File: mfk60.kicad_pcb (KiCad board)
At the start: 2 copper layers, 300 x 95.2 mm, 180 parts, among them J1 USB_C_Receptacle_USB2.0, J2 TRRS Jack, J3 ISP, J4 USB_C_Receptacle_USB2.0, J5 TRRS Jack, J6 ISP, SW1 COL1_ROW1, SW10 COL10_ROW1, SW11 COL11_ROW1, SW12 COL12_ROW1, SW13 COL13_ROW1, SW14 COL14_ROW1, SW15 COL1_ROW2, SW16 COL2_ROW2, SW17 COL3_ROW2, SW18 COL4_ROW2, SW19 COL5_ROW2, SW2 COL2_ROW1, SW20 COL6_ROW2, SW21 COL7_ROW2, SW22 COL8_ROW2, SW23 COL9_ROW2, SW24 COL10_ROW2, SW25 COL11_ROW2, SW26 COL12_ROW2, SW27 COL13_ROW2, SW28 COL14_ROW2, SW29 COL1_ROW3, SW3 COL3_ROW1, SW30 COL2_ROW3, SW31 COL3_ROW3, SW32 COL4_ROW3, SW33 COL5_ROW3, SW34 COL6_ROW3, SW35 COL7_ROW3, SW36 COL8_ROW3, SW37 COL9_ROW3, SW38 COL10_ROW3, SW39 COL11_ROW3, SW4 COL4_ROW1, SW40 COL12_ROW3, SW41 COL13_ROW3, SW42 COL1_ROW4, SW43 COL2_ROW4, SW44 COL3_ROW4, SW45 COL4_ROW4, SW46 COL5_ROW4, SW47 COL6_ROW4, SW48 COL7_ROW4, SW49 COL8_ROW4, SW5 COL5_ROW1, SW50 COL9_ROW4, SW51 COL10_ROW4, SW52 COL11_ROW4, SW53 COL12_ROW4, SW54 COL13_ROW4, SW55 COL1_ROW5, SW56 COL2_ROW5, SW57 COL3_ROW5, SW58 COL7_ROW5, SW59 COL8_ROW5, SW6 COL6_ROW1, SW60 COL9_ROW5, SW61 COL10_ROW5, SW62 RST, SW63 RST, SW7 COL7_ROW1, SW8 COL8_ROW1, SW9 COL9_ROW1, T1 Tab, T2 Tab, T3 Tab, T4 Tab, T5 Tab, T6 Tab, T7 Tab, U1 ATmega32U4-M, U2 ATmega32U4-M, Y1 16M, Y2 16M

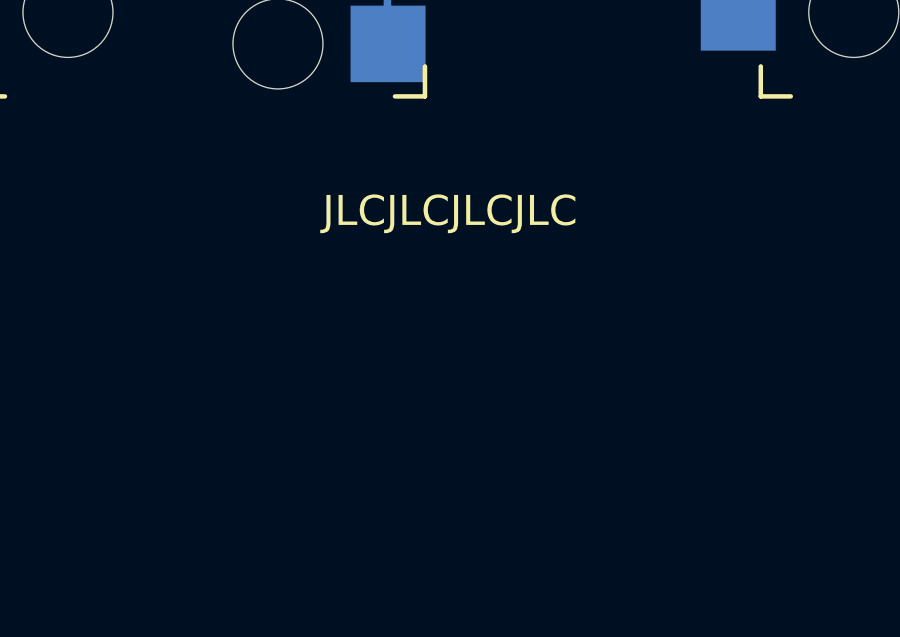
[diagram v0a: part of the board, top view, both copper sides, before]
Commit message: Adjust JLC text position and add it to script.
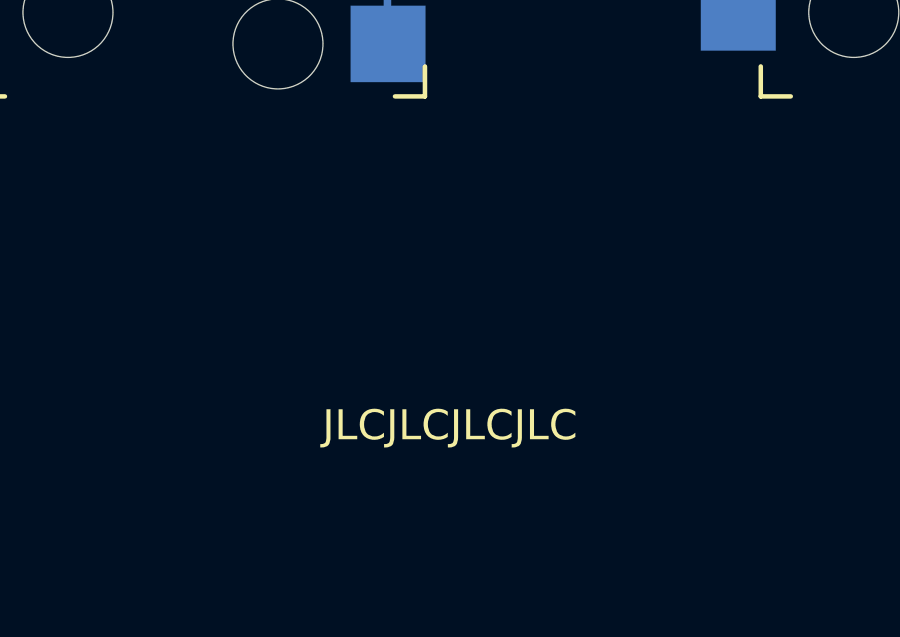
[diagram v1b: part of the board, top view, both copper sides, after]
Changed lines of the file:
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@@
     (effects (font (size 1 1) (thickness 0.15)) (justify left bottom mirror))
   )
-  (gr_text "JLCJLCJLCJLC" (at 297.653125 103.58125) (layer "F.SilkS")
+  (gr_text "JLCJLCJLCJLC" (at 297.653125 110.725) (layer "F.SilkS")
     (effects (font (size 1 1) (thickness 0.15)) (justify bottom))
   )

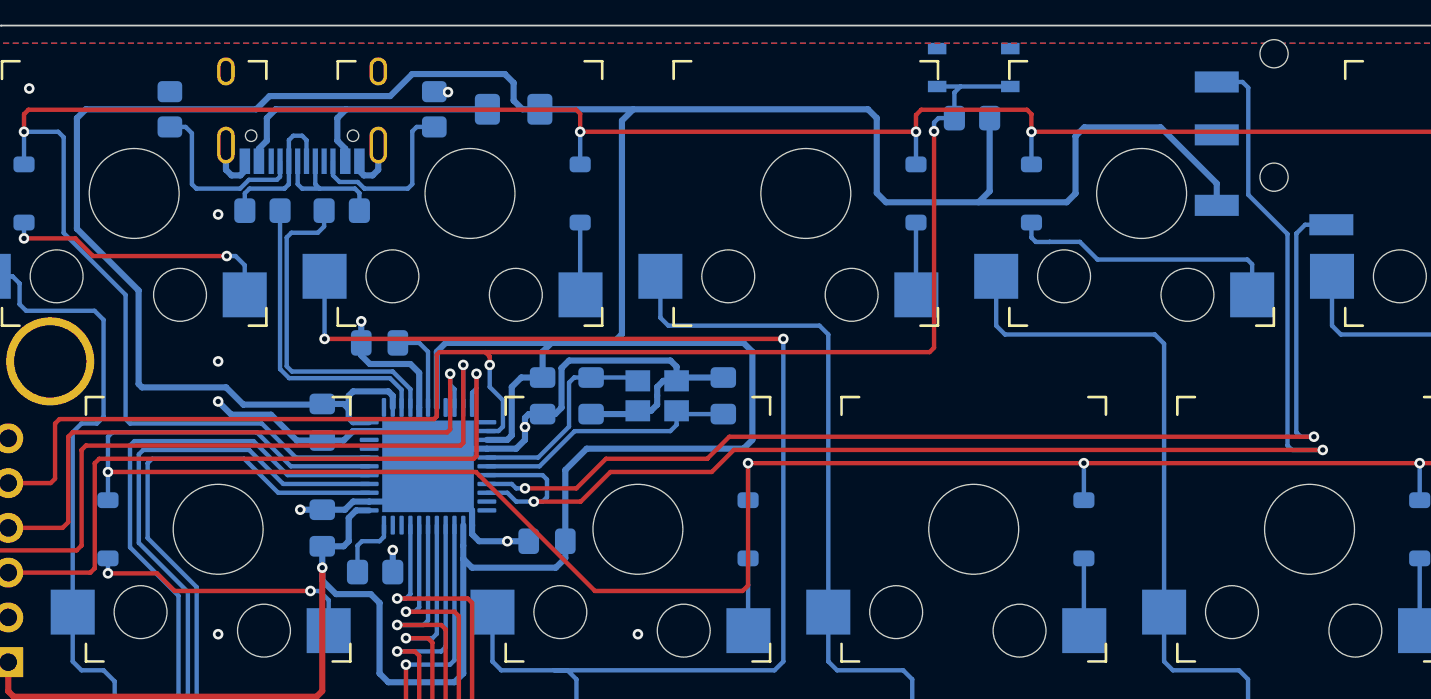
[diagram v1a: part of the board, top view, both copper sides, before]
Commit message: Add pull-up resistor on left side.
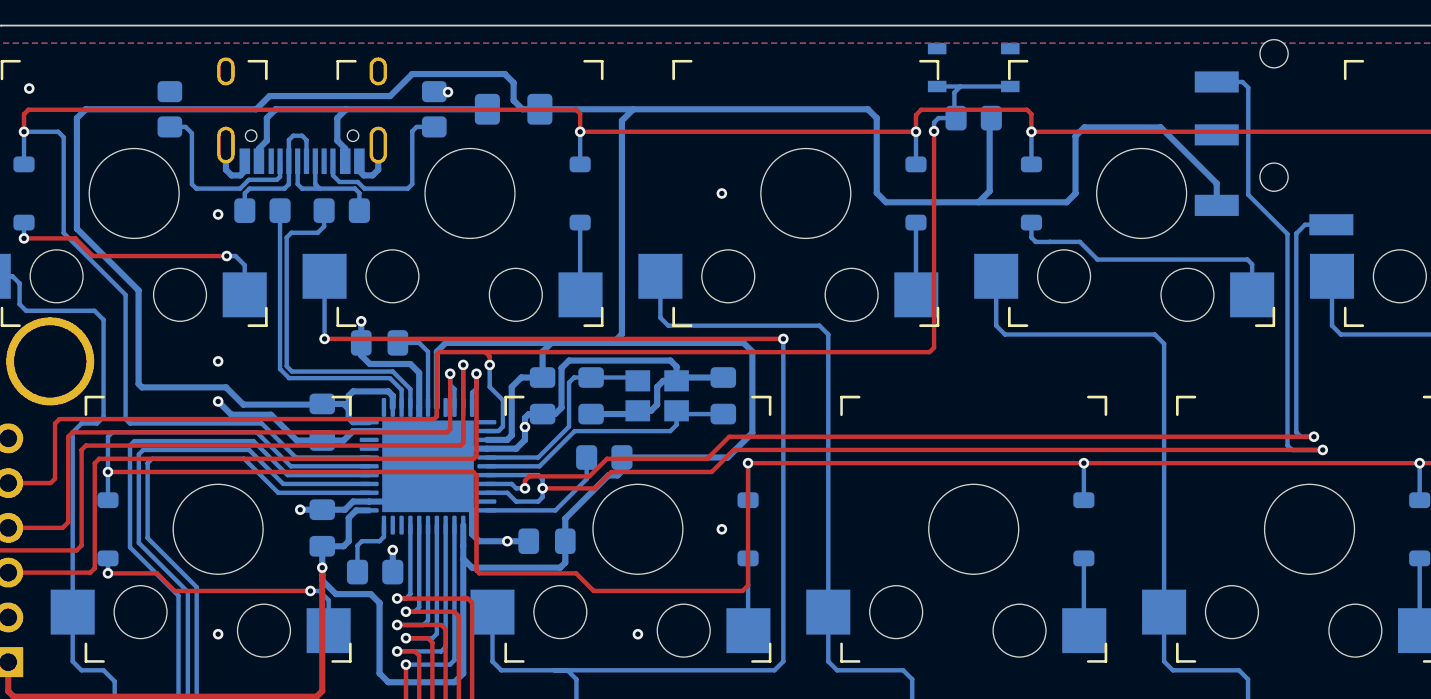
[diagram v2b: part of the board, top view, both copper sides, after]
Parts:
- added R14: 10k, Resistor_SMD:R_0805_2012Metric_Pad1.20x1.40mm_HandSolder, B.Cu at (295.6, 56.8)
- moved R7 202.3 mm to (48.2, 56.0)
- moved R13 63.3 mm to (248.8, 30.2)
- moved R6 42.6 mm to (82.2, 30.2), turned to 0 degrees
- moved R5 28.4 mm to (61.2, 49.5)
- moved R12 15.3 mm to (309.1, 49.5), turned to 180 degrees
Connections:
- R12 pad 2: Net-(U2-~{HWB}/PE2) -> R_SPLIT_HAND
- R13 pad 1: R_GND -> R_RESET
- R13 pad 2: SPLIT_HAND -> R_+5V
- R5 pad 1: RESET -> SPLIT_HAND
- R6 pad 1: GND -> RESET
- R6 pad 2: Net-(U1-~{HWB}/PE2) -> +5V
- R7 pad 1: R_RESET -> GND
- R7 pad 2: R_+5V -> Net-(U1-~{HWB}/PE2)
- U1 pad 22: unconnected-(U1-PD5-Pad22) -> SPLIT_HAND
- U2 pad 22: SPLIT_HAND -> R_SPLIT_HAND
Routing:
- net R_SPLIT_HAND: track 0.00 -> 7.74 mm
- net ROW2: track 152.2 -> 155.4 mm
- net SCL_SERIAL: track 79.5 -> 78.1 mm
- net +5V: track 243.4 -> 242.2 mm
- net GND: vias 17 -> 19

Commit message: FIX: key and diode value
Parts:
- D1: value COL1_ROW1 -> D
- D10: value COL10_ROW1 -> D
- D11: value COL11_ROW1 -> D
- D12: value COL12_ROW1 -> D
- D13: value COL13_ROW1 -> D
- D14: value COL14_ROW1 -> D
- D15: value COL1_ROW2 -> D
- D16: value COL2_ROW2 -> D
- D17: value COL3_ROW2 -> D
- D18: value COL4_ROW2 -> D
- D19: value COL5_ROW2 -> D
- D2: value COL2_ROW1 -> D
- D20: value COL6_ROW2 -> D
- D21: value COL7_ROW2 -> D
- D22: value COL8_ROW2 -> D
- D23: value COL9_ROW2 -> D
- D24: value COL10_ROW2 -> D
- D25: value COL11_ROW2 -> D
- D26: value COL12_ROW2 -> D
- D27: value COL13_ROW2 -> D
- D28: value COL14_ROW2 -> D
- D29: value COL1_ROW3 -> D
- D3: value COL3_ROW1 -> D
- D30: value COL2_ROW3 -> D
- D31: value COL3_ROW3 -> D
- D32: value COL4_ROW3 -> D
- D33: value COL5_ROW3 -> D
- D34: value COL6_ROW3 -> D
- D35: value COL7_ROW3 -> D
- D36: value COL8_ROW3 -> D
- D37: value COL9_ROW3 -> D
- D38: value COL10_ROW3 -> D
- D39: value COL11_ROW3 -> D
- D4: value COL4_ROW1 -> D
- D40: value COL12_ROW3 -> D
- D41: value COL13_ROW3 -> D
- D42: value COL1_ROW4 -> D
- D43: value COL2_ROW4 -> D
- D44: value COL3_ROW4 -> D
- D45: value COL4_ROW4 -> D
- D46: value COL5_ROW4 -> D
- D47: value COL6_ROW4 -> D
- D48: value COL7_ROW4 -> D
- D49: value COL8_ROW4 -> D
- D5: value COL5_ROW1 -> D
- D50: value COL9_ROW4 -> D
- D51: value COL10_ROW4 -> D
- D52: value COL11_ROW4 -> D
- D53: value COL12_ROW4 -> D
- D54: value COL13_ROW4 -> D
- D55: value COL1_ROW5 -> D
- D56: value COL2_ROW5 -> D
- D57: value COL3_ROW5 -> D
- D58: value COL7_ROW5 -> D
- D59: value COL8_ROW5 -> D
- D6: value COL6_ROW1 -> D
- D60: value COL9_ROW5 -> D
- D61: value COL10_ROW5 -> D
- D7: value COL7_ROW1 -> D
- D8: value COL8_ROW1 -> D
- D9: value COL9_ROW1 -> D
- SW1: value COL1_ROW1 -> KS-33
- SW10: value COL10_ROW1 -> KS-33
- SW11: value COL11_ROW1 -> KS-33
- SW12: value COL12_ROW1 -> KS-33
- SW13: value COL13_ROW1 -> KS-33
- SW14: value COL14_ROW1 -> KS-33
- SW15: value COL1_ROW2 -> KS-33
- SW16: value COL2_ROW2 -> KS-33
- SW17: value COL3_ROW2 -> KS-33
- SW18: value COL4_ROW2 -> KS-33
- SW19: value COL5_ROW2 -> KS-33
- SW2: value COL2_ROW1 -> KS-33
- SW20: value COL6_ROW2 -> KS-33
- SW21: value COL7_ROW2 -> KS-33
- SW22: value COL8_ROW2 -> KS-33
- SW23: value COL9_ROW2 -> KS-33
- SW24: value COL10_ROW2 -> KS-33
- SW25: value COL11_ROW2 -> KS-33
- SW26: value COL12_ROW2 -> KS-33
- SW27: value COL13_ROW2 -> KS-33
- SW28: value COL14_ROW2 -> KS-33
- SW29: value COL1_ROW3 -> KS-33
- SW3: value COL3_ROW1 -> KS-33
- SW30: value COL2_ROW3 -> KS-33
- SW31: value COL3_ROW3 -> KS-33
- SW32: value COL4_ROW3 -> KS-33
- SW33: value COL5_ROW3 -> KS-33
- SW34: value COL6_ROW3 -> KS-33
- SW35: value COL7_ROW3 -> KS-33
- SW36: value COL8_ROW3 -> KS-33
- SW37: value COL9_ROW3 -> KS-33
- SW38: value COL10_ROW3 -> KS-33
- SW39: value COL11_ROW3 -> KS-33
- SW4: value COL4_ROW1 -> KS-33
- SW40: value COL12_ROW3 -> KS-33
- SW41: value COL13_ROW3 -> KS-33
- SW42: value COL1_ROW4 -> KS-33
- SW43: value COL2_ROW4 -> KS-33
- SW44: value COL3_ROW4 -> KS-33
- SW45: value COL4_ROW4 -> KS-33
- SW46: value COL5_ROW4 -> KS-33
- SW47: value COL6_ROW4 -> KS-33
- SW48: value COL7_ROW4 -> KS-33
- SW49: value COL8_ROW4 -> KS-33
- SW5: value COL5_ROW1 -> KS-33
- SW50: value COL9_ROW4 -> KS-33
- SW51: value COL10_ROW4 -> KS-33
- SW52: value COL11_ROW4 -> KS-33
- SW53: value COL12_ROW4 -> KS-33
- SW54: value COL13_ROW4 -> KS-33
- SW55: value COL1_ROW5 -> KS-33
- SW56: value COL2_ROW5 -> KS-33
- SW57: value COL3_ROW5 -> KS-33
- SW58: value COL7_ROW5 -> KS-33
- SW59: value COL8_ROW5 -> KS-33
- SW6: value COL6_ROW1 -> KS-33
- SW60: value COL9_ROW5 -> KS-33
- SW61: value COL10_ROW5 -> KS-33
- SW7: value COL7_ROW1 -> KS-33
- SW8: value COL8_ROW1 -> KS-33
- SW9: value COL9_ROW1 -> KS-33
